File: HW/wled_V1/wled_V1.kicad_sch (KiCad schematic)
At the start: 25 parts, among them J1 0031.8201, U3 TXS0102DCT

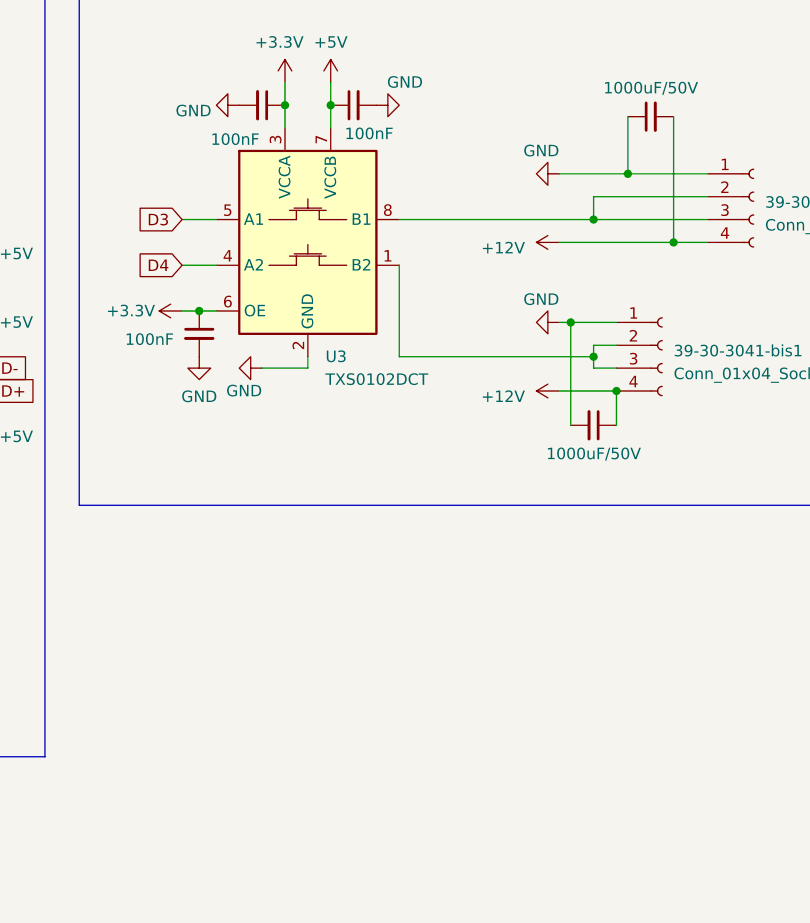
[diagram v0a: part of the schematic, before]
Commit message: nouveau level shifter + emplacement resistors. A router
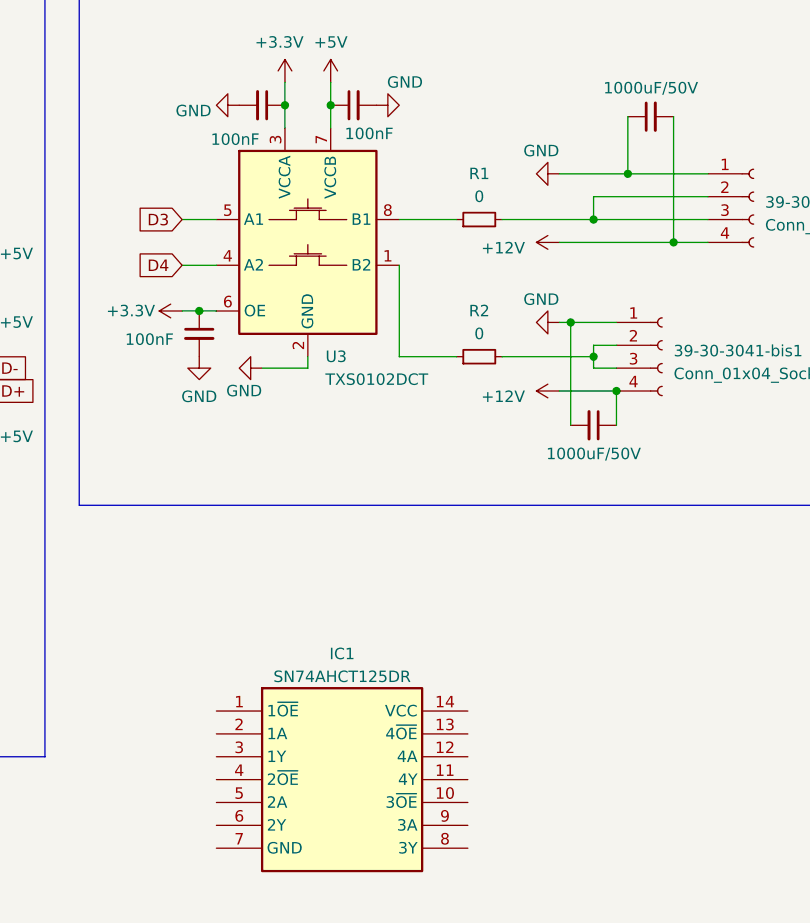
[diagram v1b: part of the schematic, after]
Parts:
- added IC1: SN74AHCT125DR, SOIC127P600X175-14N, symbol SamacSys_Parts:SN74AHCT125DR
- added R1, R2: 0, symbol Device:R_Small
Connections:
- net at 39-30-3041-bis1.2 (Pin_2), 39-30-3041-bis1.3 (Pin_3): now also R2.2; no longer U3.1 (B2)
- net at 39-30-3041.2 (Pin_2), 39-30-3041.3 (Pin_3): now also R1.2; no longer U3.8 (B1)
- new net: R2.1, U3.1 (B2)
- new net: R1.1, U3.8 (B1)
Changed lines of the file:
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@@
   (junction (at 86.36 27.94) (diameter 0) (color 0 0 0 0)
   )
-  (wire (pts (xy 316.23 58.42) (xy 337.82 58.42))
+  (wire (pts (xy 316.23 58.42) (xy 322.58 58.42))
     (stroke (width 0) (type default))
   )
@@
     (stroke (width 0) (type default))
   )
+  (wire (pts (xy 327.66 58.42) (xy 337.82 58.42))
+    (stroke (width 0) (type default))
+  )
   (wire (pts (xy 228.6 67.31) (xy 234.95 67.31))
     (stroke (width 0) (type default))
@@
     (stroke (width 0) (type default))
   )
+  (wire (pts (xy 327.66 43.18) (xy 337.82 43.18))
+    (stroke (width 0) (type default))
+  )
   (wire (pts (xy 267.97 59.69) (xy 270.51 59.69))
     (stroke (width 0) (type default))
@@
     (stroke (width 0) (type default))
   )
-  (wire (pts (xy 316.23 43.18) (xy 337.82 43.18))
+  (wire (pts (xy 316.23 43.18) (xy 322.58 43.18))
     (stroke (width 0) (type default))
   )
@@
         (path "/de2f0c7b-62aa-45a1-944c-ab4e5150c860"
           (reference "#PWR034") (unit 1)
+        )
+      )
+    )
+  )
+  (symbol (lib_id "Device:R_Small") (at 325.12 58.42 90) (unit 1)
+    (in_bom yes) (on_board yes) (dnp no) (fields_autoplaced)
+    (property "Reference" "R2" (at 325.12 53.34 90)
+      (effects (font (size 1.27 1.27)))
+    )
+    (property "Value" "0" (at 325.12 55.88 90)
+      (effects (font (size 1.27 1.27)))
+    )
+    (property "Footprint" "" (at 325.12 58.42 0)
+      (effects (font (size 1.27 1.27)) hide)
+    )
+    (property "Datasheet" "~" (at 325.12 58.42 0)
+      (effects (font (size 1.27 1.27)) hide)
+    )
+    (pin "1")
+    (pin "2")
+    (instances
+      (project "wled_V1"
+        (path "/de2f0c7b-62aa-45a1-944c-ab4e5150c860"
+          (reference "R2") (unit 1)
         )
       )
@@
     )
   )
+  (symbol (lib_id "Device:R_Small") (at 325.12 43.18 90) (unit 1)
+    (in_bom yes) (on_board yes) (dnp no) (fields_autoplaced)
+    (property "Reference" "R1" (at 325.12 38.1 90)
+      (effects (font (size 1.27 1.27)))
+    )
+    (property "Value" "0" (at 325.12 40.64 90)
+      (effects (font (size 1.27 1.27)))
+    )
+    (property "Footprint" "" (at 325.12 43.18 0)
+      (effects (font (size 1.27 1.27)) hide)
+    )
+    (property "Datasheet" "~" (at 325.12 43.18 0)
+      (effects (font (size 1.27 1.27)) hide)
+    )
+    (pin "1")
+    (pin "2")
+    (instances
+      (project "wled_V1"
+        (path "/de2f0c7b-62aa-45a1-944c-ab4e5150c860"
+          (reference "R1") (unit 1)
+        )
+      )
+    )
+  )
   (symbol (lib_id "power:GND") (at 334.01 54.61 270) (unit 1)
     (in_bom yes) (on_board yes) (dnp no)
@@
         )
       )
+    )
+  )
+  (symbol (lib_id "SamacSys_Parts:SN74AHCT125DR") (at 295.91 97.79 0) (unit 1)
+    (in_bom yes) (on_board yes) (dnp no) (fields_autoplaced)
+    (property "Reference" "IC1" (at 309.88 91.44 0)
+      (effects (font (size 1.27 1.27)))
+    )
+    (property "Value" "SN74AHCT125DR" (at 309.88 93.98 0)
+      (effects (font (size 1.27 1.27)))
+    )
+    (property "Footprint" "SOIC127P600X175-14N" (at 320.04 192.71 0)
+      (effects (font (size 1.27 1.27)) (justify left top) hide)
+    )
+    (property "Datasheet" "http://www.ti.com/lit/gpn/sn74ahct125" (at 320.04 292.71 0)
+      (effects (font (size 1.27 1.27)) (justify left top) hide)
+    )
+    (property "Height" "1.75" (at 320.04 492.71 0)
+      (effects (font (size 1.27 1.27)) (justify left top) hide)
+    )
+    (property "Mouser Part Number" "595-SN74AHCT125DR" (at 320.04 592.71 0)
+      (effects (font (size 1.27 1.27)) (justify left top) hide)
+    )
+    (property "Mouser Price/Stock" "https://www.mouser.co.uk/ProductDetail/Texas-Instruments/SN74AHCT125DR?qs=B7lSdIxWQkm9VQkJOjfRaA%3D%3D" (at 320.04 692.71 0)
+      (effects (font (size 1.27 1.27)) (justify left top) hide)
+    )
+    (property "Manufacturer_Name" "Texas Instruments" (at 320.04 792.71 0)
+      (effects (font (size 1.27 1.27)) (justify left top) hide)
+    )
+    (property "Manufacturer_Part_Number" "SN74AHCT125DR" (at 320.04 892.71 0)
+      (effects (font (size 1.27 1.27)) (justify left top) hide)
+    )
+    (pin "1")
+    (pin "10")
+    (pin "11")
+    (pin "12")
+    (pin "13")
+    (pin "14")
+    (pin "2")
+    (pin "3")
+    (pin "4")
+    (pin "5")
+    (pin "6")
+    (pin "7")
+    (pin "8")
+    (pin "9")
+    (instances
+      (project "wled_V1"
+        (path "/de2f0c7b-62aa-45a1-944c-ab4e5150c860"
+          (reference "IC1") (unit 1)
+        )
+      )

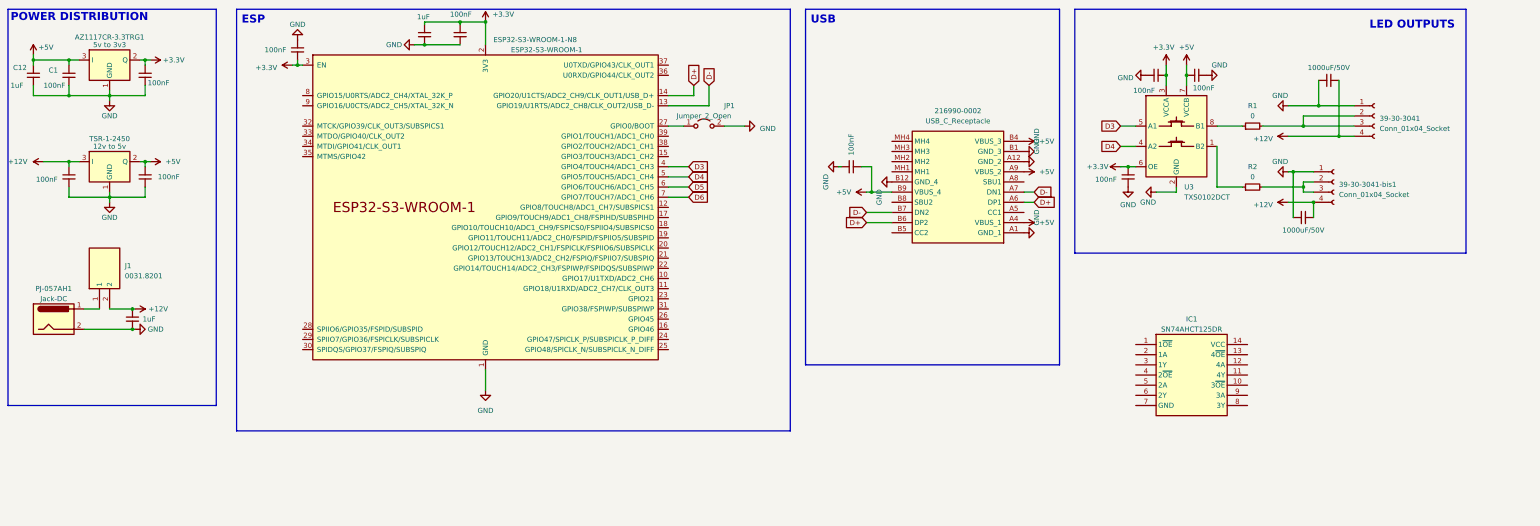
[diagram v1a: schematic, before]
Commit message: new parts and routing
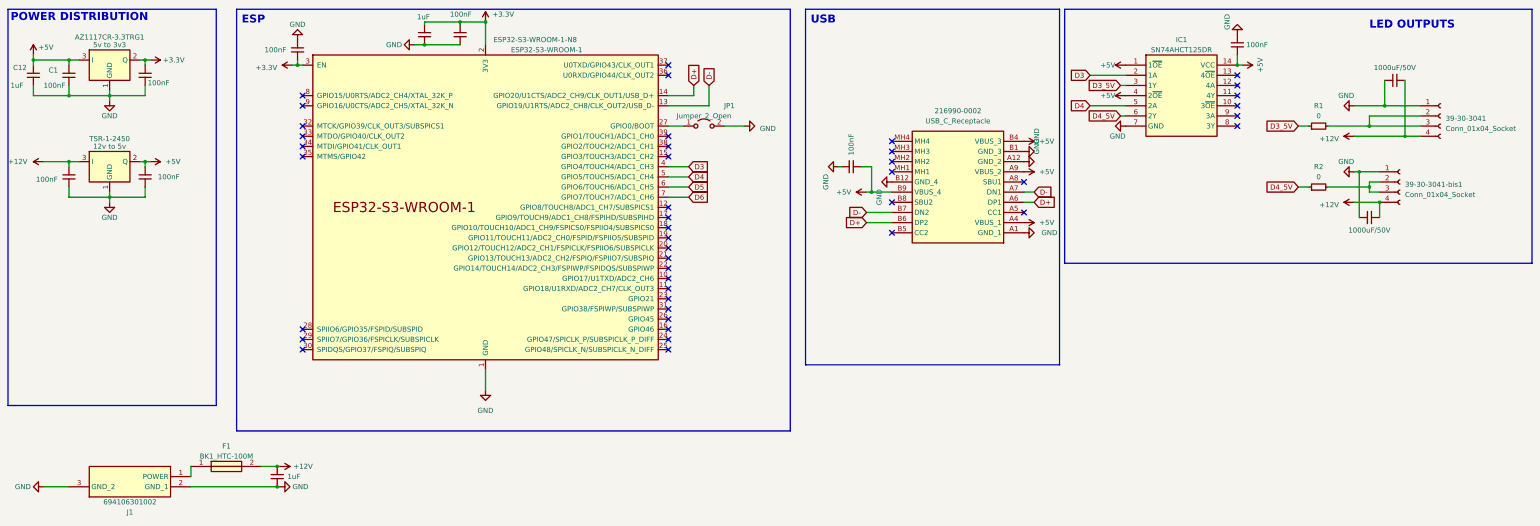
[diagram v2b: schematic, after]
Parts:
- removed C10, C15: 100nF, SamacSys_Parts:CAPC1005X55N, symbol Device:C_Small
- removed J1: 0031.8201, SamacSys_Parts:0031.8201, symbol SamacSys_Parts:0031.8201
- removed PJ-057AH1: Jack-DC, SamacSys_Parts:PJ057AH, symbol Connector:Jack-DC
- removed U3: TXS0102DCT, Package_SO:SSOP-8_2.95x2.8mm_P0.65mm, symbol Logic_LevelTranslator:TXS0102DCT
- added F1: BK1_HTC-100M, SamacSys_Parts:BK1HTC100M, symbol SamacSys_Parts:BK1_HTC-100M
- added J1: 694106301002, SamacSys_Parts:694106301002_1, symbol SamacSys_Parts:694106301002
- AZ1117CR-3.3TRG1: footprint Package_TO_SOT_SMD:TO-252-3_TabPin2 -> SamacSys_Parts:AZ1117CR33TRG1
- C5, C8: footprint SamacSys_Parts:CAPAE1030X1030N -> SamacSys_Parts:CAPAE1030X1050N
- IC1: footprint SOIC127P600X175-14N -> SamacSys_Parts:SOIC127P600X175-14N
- R1, R2: footprint (none) -> Resistor_SMD:R_0603_1608Metric_Pad0.98x0.95mm_HandSolder
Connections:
- net +12V: now also F1.2
- net +5V: now also IC1.1 (1~{OE}), IC1.14 (VCC), IC1.4 (2~{OE})
- net D3: now also IC1.2 (1A)
- net D4: now also IC1.5 (2A)
- net GND: now also IC1.7 (GND), J1.2 (GND_1), J1.3 (GND_2)
- net D4_5V: now reaches R2.1
- net D4_5V: now also IC1.6 (2Y)
- net D3_5V: now reaches R1.1
- net D3_5V: now also IC1.3 (1Y)
- new net: F1.1, J1.1 (POWER)
- no-connect marks 0 -> 43
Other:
- moved on the sheet: 39-30-3041, 39-30-3041-bis1, IC1, R1, R2

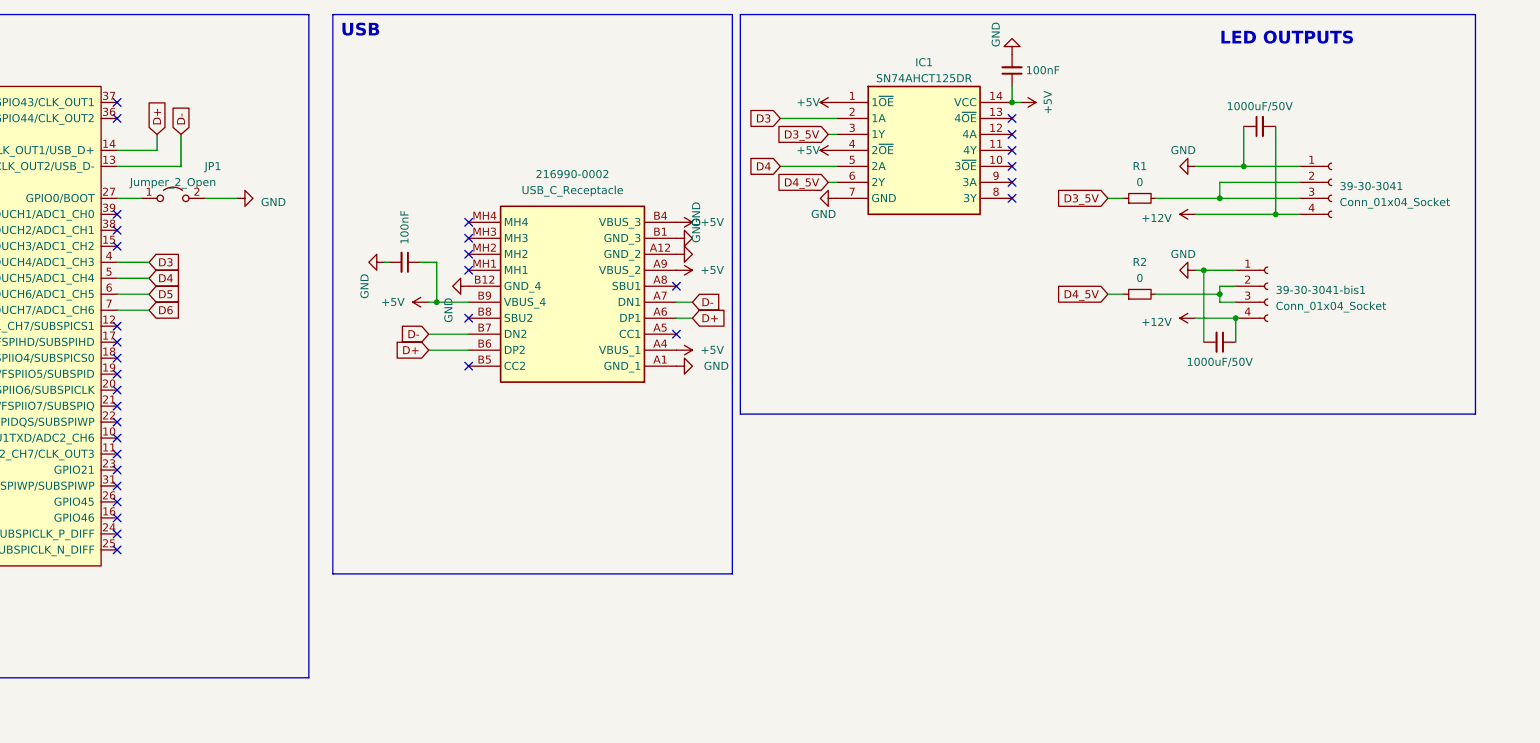
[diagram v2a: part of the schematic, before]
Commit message: added relay
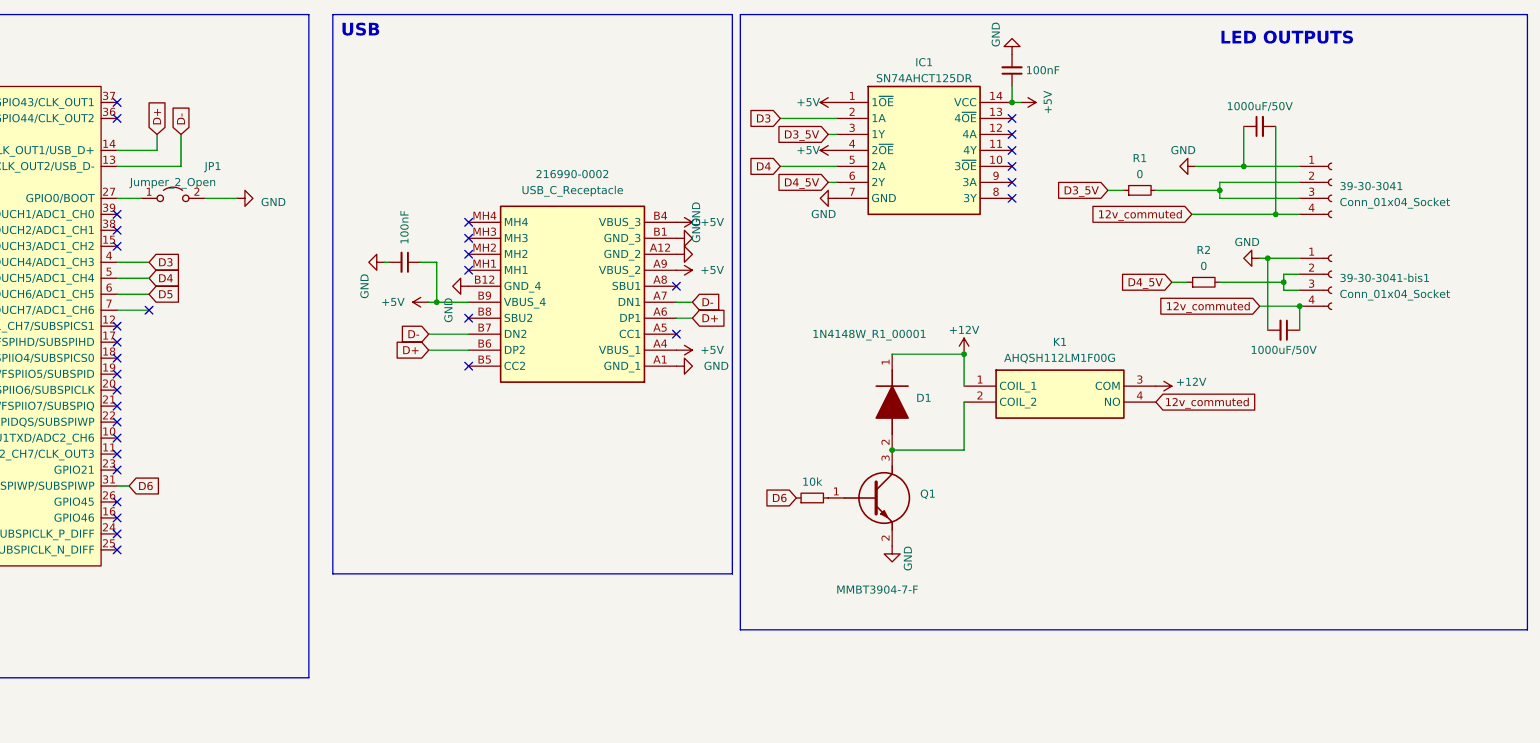
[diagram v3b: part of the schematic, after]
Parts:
- added D1: 1N4148W_R1_00001, SOD3816X135N, symbol SamacSys_Parts:1N4148W_R1_00001
- added K1: AHQSH112LM1F00G, AHQSH112LM1F00G, symbol SamacSys_Parts:AHQSH112LM1F00G
- added Q1: MMBT3904-7-F, SOT96P240X110-3N, symbol SamacSys_Parts:MMBT3904-7-F
- added RN73H1JTTD1002F50: 10k, Resistor_SMD:R_0603_1608Metric_Pad0.98x0.95mm_HandSolder, symbol Device:R_Small
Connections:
- net +12V: now also D1.1 (K), K1.1 (COIL_1), K1.3 (COM); no longer 39-30-3041-bis1.4 (Pin_4), 39-30-3041.4 (Pin_4), C5.1, C8.2
- net D6: now also ESP32-S3-WROOM-1-N8.31 (GPIO38/FSPIWP/SUBSPIWP), RN73H1JTTD1002F50.1; no longer ESP32-S3-WROOM-1-N8.7 (GPIO7/TOUCH7/ADC1_CH6)
- net GND: now also Q1.2 (E)
- new net: Q1.1 (B), RN73H1JTTD1002F50.2
- new net: D1.2 (A), K1.2 (COIL_2), Q1.3 (C)
- new net 12v_commuted: 39-30-3041-bis1.4 (Pin_4), 39-30-3041.4 (Pin_4), C5.1, C8.2, K1.4 (NO)
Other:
- moved on the sheet: 39-30-3041-bis1, R1, R2
